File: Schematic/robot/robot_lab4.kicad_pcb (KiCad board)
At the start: 2 copper layers, 21 parts, among them J1 Conn_02x10_Counter_Clockwise, J2 Conn_02x08_Top_Bottom, J4 Conn_02x08_Top_Bottom, J5 Conn_02x06_Counter_Clockwise, J6 Encoder_Right, J7 Motor_Driver, J8 Encoder_Left, J9 IR_Distance_Sensor, SW1 SW_MEC_5E, U1 L298HN, U2 HC-SR04, U3 TSSP58P38

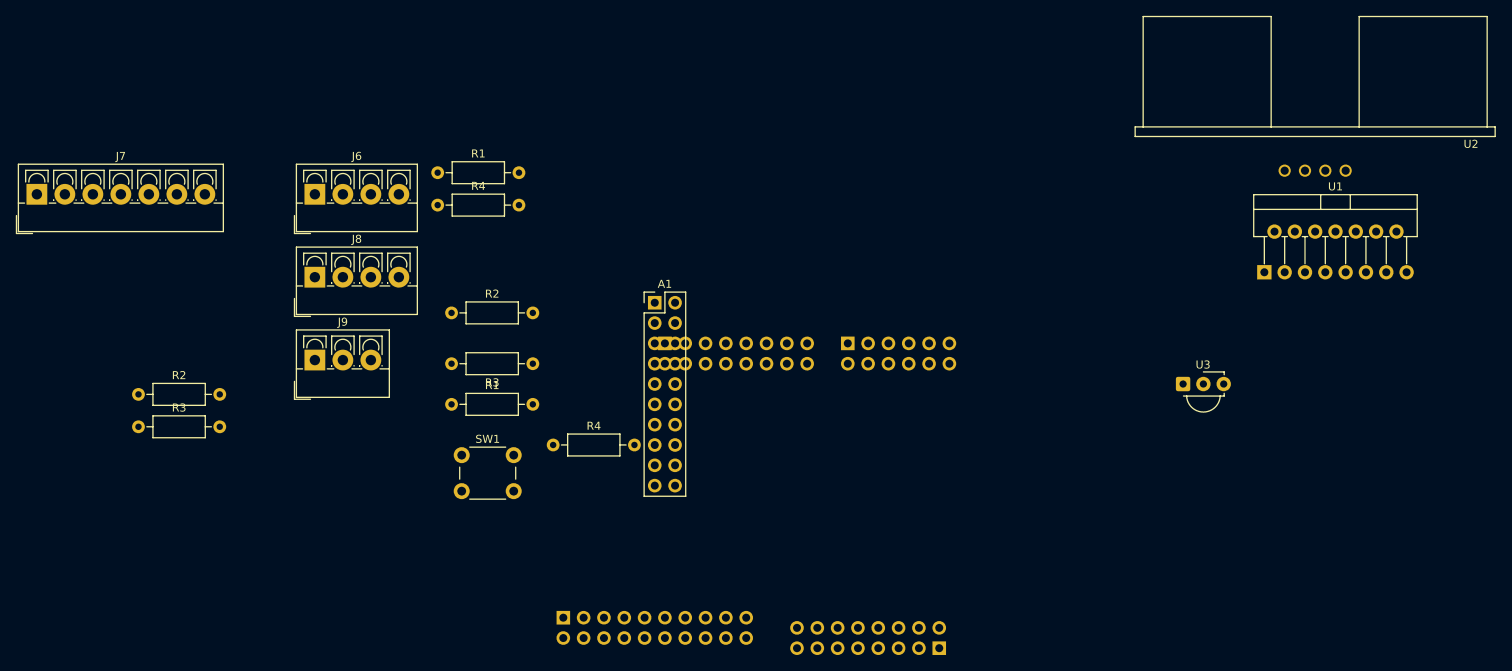
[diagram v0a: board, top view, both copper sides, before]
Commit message: Edited layout but headers on wrong side
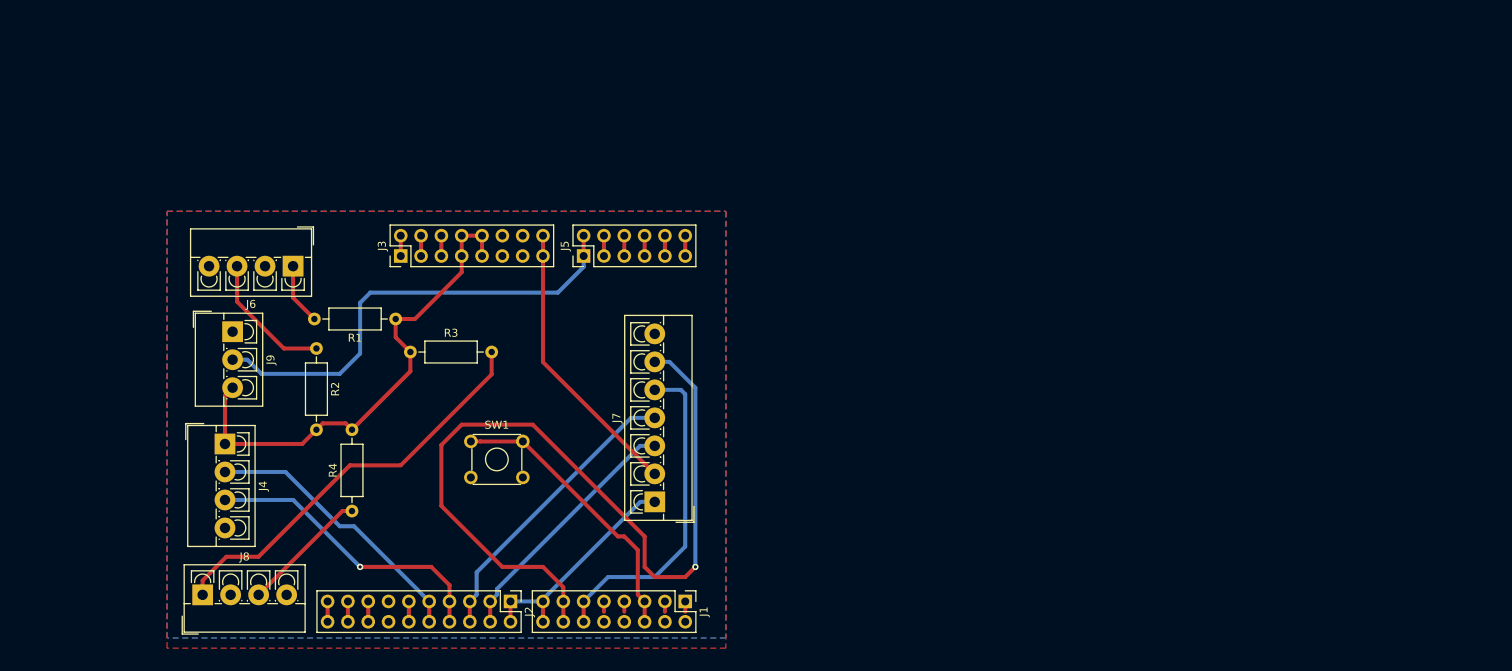
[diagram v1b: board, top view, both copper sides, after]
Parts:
- removed A1: Arduino_UNO_R3, Connector_PinHeader_2.54mm:PinHeader_2x10_P2.54mm_Vertical
- removed the R1 at (82.5, 81.3)
- removed the R1 at (80.8, 52.3)
- removed the R2 at (82.5, 69.8)
- removed the R2 at (43.4, 80.0)
- removed the R3 at (92.7, 76.2)
- removed the R3 at (43.4, 84.1)
- removed the R4 at (95.2, 86.4)
- removed the R4 at (80.8, 56.4)
- removed U1: L298HN, Package_TO_SOT_THT:TO-220-15_P2.54x2.54mm_StaggerOdd_Lead4.58mm_Vertical
- removed U2: HC-SR04, Schematic:XCVR_HC-SR04
- removed U3: TSSP58P38, OptoDevice:Vishay_MINICAST-3Pin
- added J3: Conn_02x08_Odd_Even, Connector_PinHeader_2.54mm:PinHeader_2x08_P2.54mm_Vertical, F.Cu at (76.2, 62.7)
- added R1: 330, Resistor_THT:R_Axial_DIN0207_L6.3mm_D2.5mm_P10.16mm_Horizontal, F.Cu at (75.6, 70.6)
- added R2: 10k, Resistor_THT:R_Axial_DIN0207_L6.3mm_D2.5mm_P10.16mm_Horizontal, F.Cu at (65.7, 74.3)
- added R3: 330, Resistor_THT:R_Axial_DIN0207_L6.3mm_D2.5mm_P10.16mm_Horizontal, F.Cu at (77.4, 74.7)
- added R4: 10k, Resistor_THT:R_Axial_DIN0207_L6.3mm_D2.5mm_P10.16mm_Horizontal, F.Cu at (70.1, 94.6)
- J1: value Conn_02x10_Counter_Clockwise -> Conn_02x08_Odd_Even; footprint Connector_PinHeader_2.54mm:PinHeader_2x10_P2.54mm_Vertical -> Connector_PinHeader_2.54mm:PinHeader_2x08_P2.54mm_Vertical; moved to F.Cu
- J2: value Conn_02x08_Top_Bottom -> Conn_02x10_Odd_Even_MountingPin; footprint Connector_PinHeader_2.54mm:PinHeader_2x08_P2.54mm_Vertical -> Connector_PinHeader_2.54mm:PinHeader_2x10_P2.54mm_Vertical; moved to F.Cu
- J4: value Conn_02x08_Top_Bottom -> HC-SR04; footprint Connector_PinHeader_2.54mm:PinHeader_2x08_P2.54mm_Vertical -> TerminalBlock_4Ucon:TerminalBlock_4Ucon_1x04_P3.50mm_Vertical; moved to F.Cu
- J5: value Conn_02x06_Counter_Clockwise -> Conn_02x06_Odd_Even; moved to F.Cu
- SW1: footprint Button_Switch_THT:SW_PUSH_6mm -> Button_Switch_THT:SW_TH_Tactile_Omron_B3F-10xx
- moved J7 86.3 mm to (108.0, 93.5), turned to 90 degrees
- moved J4 56.4 mm to (54.2, 86.2)
- moved J2 53.9 mm to (89.9, 105.9), turned to 270 degrees
- moved J8 42.1 mm to (51.4, 105.1)
- moved J5 34.8 mm to (99.1, 62.7), turned to 90 degrees
- moved J1 15.4 mm to (111.8, 105.9)
- moved J9 10.9 mm to (55.2, 72.2), turned to 270 degrees
- moved J6 9.39 mm to (62.7, 64.0), turned to 180 degrees
- moved SW1 2.06 mm to (85.0, 85.9)
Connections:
- J1 pad 1: 5V -> Net-(J1-Pad1)
- J1 pad 11: Net-(J1-Pad10) -> PIN_5
- J1 pad 12: Net-(J1-Pad12) -> PIN_5
- J1 pad 13: Net-(J1-Pad13) -> PIN_6
- J1 pad 14: GND -> PIN_6
- J1 pad 15: Net-(J1-Pad15) -> 5V
- J1 pad 16: Net-(J1-Pad16) -> 5V
- J1 pad 2: PIN_9 -> Net-(J1-Pad1)
- J1 pad 3: PIN_10 -> Net-(J1-Pad3)
- J1 pad 4: Net-(J1-Pad17) -> Net-(J1-Pad3)
- J1 pad 5: Net-(J1-Pad16) -> PIN_2
- J1 pad 6: Net-(J1-Pad15) -> PIN_2
- J1 pad 7: GND -> Net-(J1-Pad7)
- J1 pad 8: Net-(J1-Pad13) -> Net-(J1-Pad7)
- J1 pad 9: Net-(J1-Pad12) -> Net-(J1-Pad10)
- J2 pad 1: (no net) -> 5V
- J2 pad 10: Net-(J2-Pad10) -> PIN_12
- J2 pad 12: Net-(J2-Pad12) -> Net-(J2-Pad11)
- J2 pad 13: Net-(J2-Pad13) -> GND
- J2 pad 14: PIN_5 -> GND
- J2 pad 15: PIN_6 -> Net-(J2-Pad15)
- J2 pad 16: 5V -> Net-(J2-Pad15)
- J2 pad 2: Net-(J2-Pad10) -> 5V
- J2 pad 3: Net-(J2-Pad11) -> PIN_9
- J2 pad 4: Net-(J2-Pad12) -> PIN_9
- J2 pad 5: Net-(J2-Pad13) -> PIN_10
- J2 pad 6: PIN_5 -> PIN_10
- J2 pad 7: PIN_6 -> PIN_11
- J2 pad 8: 5V -> PIN_11
- J2 pad 9: (no net) -> PIN_12
- J4 pad 1: Net-(J4-Pad1) -> 5V
- J4 pad 2: Net-(J4-Pad10) -> PIN_12
- J4 pad 3: Net-(J4-Pad11) -> PIN_11
- J4 pad 4: 5V -> GND
- J5 pad 1: Net-(A1-Pad9) -> PIN_A0
- J5 pad 10: Net-(A1-Pad11) -> Net-(J5-Pad10)
- J5 pad 11: Net-(A1-Pad10) -> Net-(J5-Pad11)
- J5 pad 12: Net-(A1-Pad9) -> Net-(J5-Pad11)
- J5 pad 2: Net-(A1-Pad10) -> PIN_A0
- J5 pad 3: Net-(A1-Pad11) -> Net-(J5-Pad3)
- J5 pad 4: Net-(A1-Pad12) -> Net-(J5-Pad3)
- J5 pad 5: Net-(A1-Pad13) -> Net-(J5-Pad5)
- J5 pad 6: Net-(A1-Pad14) -> Net-(J5-Pad5)
- J5 pad 7: Net-(A1-Pad14) -> Net-(J5-Pad7)
- J5 pad 8: Net-(A1-Pad13) -> Net-(J5-Pad7)
- J5 pad 9: Net-(A1-Pad12) -> Net-(J5-Pad10)
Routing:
- net PIN_6: track 0.00 -> 103.6 mm, vias 0 -> 1
- net 5V: track 0.00 -> 91.1 mm
- net PIN_A0: track 0.00 -> 57.8 mm
- net Net-(J8-Pad1): track 0.00 -> 51.4 mm
- net PIN_5: track 0.00 -> 41.2 mm
- net PIN_11: track 0.00 -> 37.1 mm, vias 0 -> 1
- net PIN_10: track 0.00 -> 36.8 mm
- net PIN_2: track 0.00 -> 35.8 mm
- net VIN: track 0.00 -> 35.6 mm
- net PIN_12: track 0.00 -> 34.8 mm
- net PIN_9: track 0.00 -> 31.6 mm
- net Net-(J6-Pad3): track 0.00 -> 16.8 mm
- net Net-(J8-Pad3): track 0.00 -> 16.0 mm
- net Net-(J6-Pad1): track 0.00 -> 7.71 mm
- net Net-(J5-Pad7): track 0.00 -> 2.54 mm
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- added copper zone on B.Cu, net GND
- added copper zone on F.Cu, net GND
